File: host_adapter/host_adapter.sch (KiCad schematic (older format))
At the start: 7 parts, among them J1 Conn_01x40_Male, J2 Conn_01x40_Male, J3 Conn_01x02_Male, J4 Connector_PCIe_x16, J5 Conn_01x40_Male, J6 Conn_01x40_Male, J7 Conn_01x02_Male

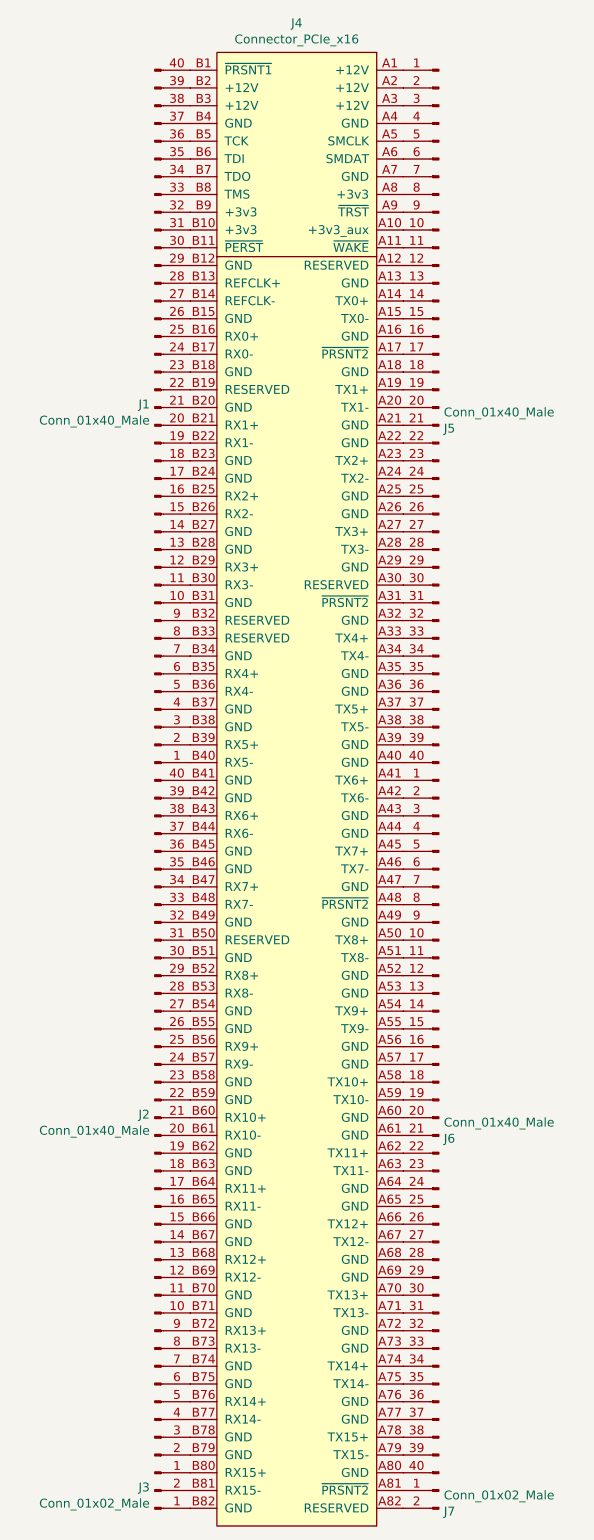
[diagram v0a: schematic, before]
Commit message: Deepen PCIe x16 slot cutout
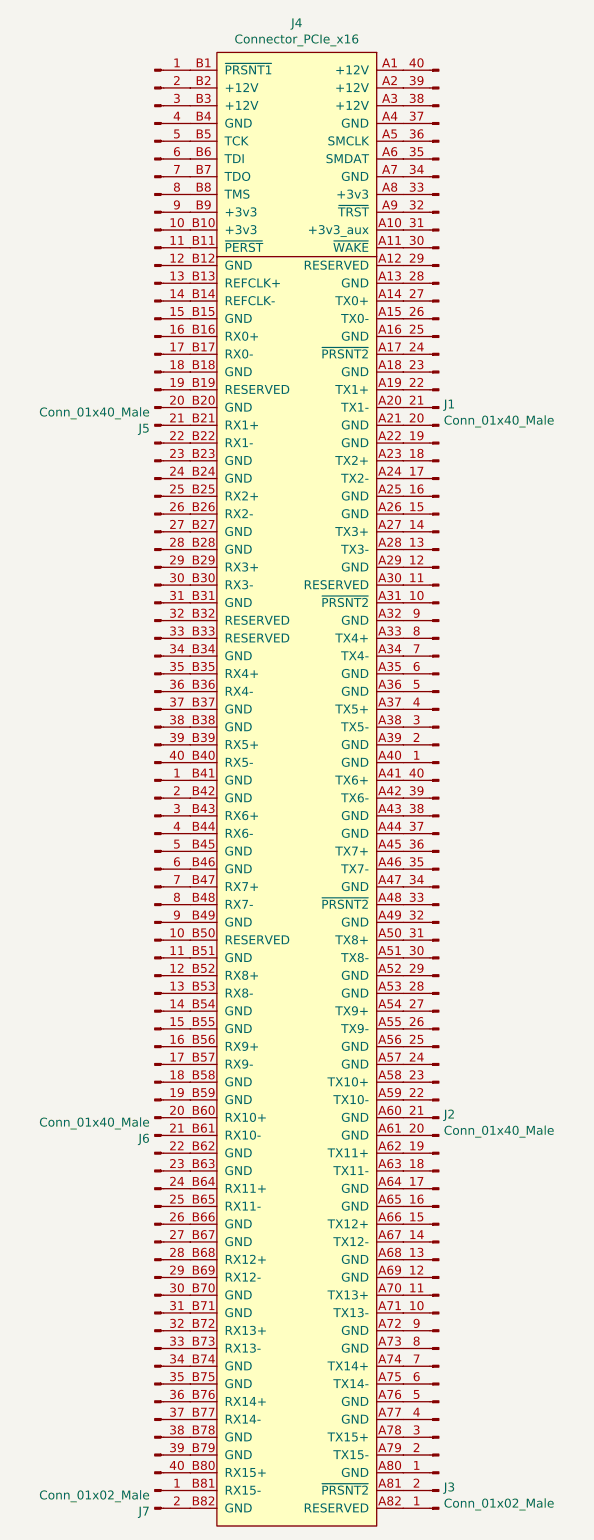
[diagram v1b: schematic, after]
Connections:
- net at J4.A1 (+12V): now also J1.40 (Pin_40); no longer J5.1 (Pin_1)
- net at J4.A10 (+3v3_aux): now also J1.31 (Pin_31); no longer J5.10 (Pin_10)
- net at J4.A11 (~WAKE): now also J1.30 (Pin_30); no longer J5.11 (Pin_11)
- net at J4.A12 (RESERVED): now also J1.29 (Pin_29); no longer J5.12 (Pin_12)
- net at J4.A13 (GND): now also J1.28 (Pin_28); no longer J5.13 (Pin_13)
- net at J4.A14 (TX0+): now also J1.27 (Pin_27); no longer J5.14 (Pin_14)
- net at J4.A15 (TX0-): now also J1.26 (Pin_26); no longer J5.15 (Pin_15)
- net at J4.A16 (GND): now also J1.25 (Pin_25); no longer J5.16 (Pin_16)
- net at J4.A17 (~PRSNT2): now also J1.24 (Pin_24); no longer J5.17 (Pin_17)
- net at J4.A18 (GND): now also J1.23 (Pin_23); no longer J5.18 (Pin_18)
- net at J4.A19 (TX1+): now also J1.22 (Pin_22); no longer J5.19 (Pin_19)
- net at J4.A2 (+12V): now also J1.39 (Pin_39); no longer J5.2 (Pin_2)
- net at J4.A20 (TX1-): now also J1.21 (Pin_21); no longer J5.20 (Pin_20)
- net at J4.A21 (GND): now also J1.20 (Pin_20); no longer J5.21 (Pin_21)
- net at J4.A22 (GND): now also J1.19 (Pin_19); no longer J5.22 (Pin_22)
- net at J4.A23 (TX2+): now also J1.18 (Pin_18); no longer J5.23 (Pin_23)
- net at J4.A24 (TX2-): now also J1.17 (Pin_17); no longer J5.24 (Pin_24)
- net at J4.A25 (GND): now also J1.16 (Pin_16); no longer J5.25 (Pin_25)
- net at J4.A26 (GND): now also J1.15 (Pin_15); no longer J5.26 (Pin_26)
- net at J4.A27 (TX3+): now also J1.14 (Pin_14); no longer J5.27 (Pin_27)
- net at J4.A28 (TX3-): now also J1.13 (Pin_13); no longer J5.28 (Pin_28)
- net at J4.A29 (GND): now also J1.12 (Pin_12); no longer J5.29 (Pin_29)
- net at J4.A3 (+12V): now also J1.38 (Pin_38); no longer J5.3 (Pin_3)
- net at J4.A30 (RESERVED): now also J1.11 (Pin_11); no longer J5.30 (Pin_30)
- net at J4.A31 (~PRSNT2): now also J1.10 (Pin_10); no longer J5.31 (Pin_31)
- net at J4.A32 (GND): now also J1.9 (Pin_9); no longer J5.32 (Pin_32)
- net at J4.A33 (TX4+): now also J1.8 (Pin_8); no longer J5.33 (Pin_33)
- net at J4.A34 (TX4-): now also J1.7 (Pin_7); no longer J5.34 (Pin_34)
- net at J4.A35 (GND): now also J1.6 (Pin_6); no longer J5.35 (Pin_35)
- net at J4.A36 (GND): now also J1.5 (Pin_5); no longer J5.36 (Pin_36)
- net at J4.A37 (TX5+): now also J1.4 (Pin_4); no longer J5.37 (Pin_37)
- net at J4.A38 (TX5-): now also J1.3 (Pin_3); no longer J5.38 (Pin_38)
- net at J4.A39 (GND): now also J1.2 (Pin_2); no longer J5.39 (Pin_39)
- net at J4.A4 (GND): now also J1.37 (Pin_37); no longer J5.4 (Pin_4)
- net at J4.A40 (GND): now also J1.1 (Pin_1); no longer J5.40 (Pin_40)
- net at J4.A41 (TX6+): now also J2.40 (Pin_40); no longer J6.1 (Pin_1)
- net at J4.A42 (TX6-): now also J2.39 (Pin_39); no longer J6.2 (Pin_2)
- net at J4.A43 (GND): now also J2.38 (Pin_38); no longer J6.3 (Pin_3)
- net at J4.A44 (GND): now also J2.37 (Pin_37); no longer J6.4 (Pin_4)
- net at J4.A45 (TX7+): now also J2.36 (Pin_36); no longer J6.5 (Pin_5)
- net at J4.A46 (TX7-): now also J2.35 (Pin_35); no longer J6.6 (Pin_6)
- net at J4.A47 (GND): now also J2.34 (Pin_34); no longer J6.7 (Pin_7)
- net at J4.A48 (~PRSNT2): now also J2.33 (Pin_33); no longer J6.8 (Pin_8)
- net at J4.A49 (GND): now also J2.32 (Pin_32); no longer J6.9 (Pin_9)
- net at J4.A5 (SMCLK): now also J1.36 (Pin_36); no longer J5.5 (Pin_5)
- net at J4.A50 (TX8+): now also J2.31 (Pin_31); no longer J6.10 (Pin_10)
- net at J4.A51 (TX8-): now also J2.30 (Pin_30); no longer J6.11 (Pin_11)
- net at J4.A52 (GND): now also J2.29 (Pin_29); no longer J6.12 (Pin_12)
- net at J4.A53 (GND): now also J2.28 (Pin_28); no longer J6.13 (Pin_13)
- net at J4.A54 (TX9+): now also J2.27 (Pin_27); no longer J6.14 (Pin_14)
- net at J4.A55 (TX9-): now also J2.26 (Pin_26); no longer J6.15 (Pin_15)
- net at J4.A56 (GND): now also J2.25 (Pin_25); no longer J6.16 (Pin_16)
- net at J4.A57 (GND): now also J2.24 (Pin_24); no longer J6.17 (Pin_17)
- net at J4.A58 (TX10+): now also J2.23 (Pin_23); no longer J6.18 (Pin_18)
- net at J4.A59 (TX10-): now also J2.22 (Pin_22); no longer J6.19 (Pin_19)
- net at J4.A6 (SMDAT): now also J1.35 (Pin_35); no longer J5.6 (Pin_6)
- net at J4.A60 (GND): now also J2.21 (Pin_21); no longer J6.20 (Pin_20)
- net at J4.A61 (GND): now also J2.20 (Pin_20); no longer J6.21 (Pin_21)
- net at J4.A62 (TX11+): now also J2.19 (Pin_19); no longer J6.22 (Pin_22)
- net at J4.A63 (TX11-): now also J2.18 (Pin_18); no longer J6.23 (Pin_23)
- net at J4.A64 (GND): now also J2.17 (Pin_17); no longer J6.24 (Pin_24)
- net at J4.A65 (GND): now also J2.16 (Pin_16); no longer J6.25 (Pin_25)
- net at J4.A66 (TX12+): now also J2.15 (Pin_15); no longer J6.26 (Pin_26)
- net at J4.A67 (TX12-): now also J2.14 (Pin_14); no longer J6.27 (Pin_27)
- net at J4.A68 (GND): now also J2.13 (Pin_13); no longer J6.28 (Pin_28)
- net at J4.A69 (GND): now also J2.12 (Pin_12); no longer J6.29 (Pin_29)
- net at J4.A7 (GND): now also J1.34 (Pin_34); no longer J5.7 (Pin_7)
- net at J4.A70 (TX13+): now also J2.11 (Pin_11); no longer J6.30 (Pin_30)
- net at J4.A71 (TX13-): now also J2.10 (Pin_10); no longer J6.31 (Pin_31)
- net at J4.A72 (GND): now also J2.9 (Pin_9); no longer J6.32 (Pin_32)
- net at J4.A73 (GND): now also J2.8 (Pin_8); no longer J6.33 (Pin_33)
- net at J4.A74 (TX14+): now also J2.7 (Pin_7); no longer J6.34 (Pin_34)
- net at J4.A75 (TX14-): now also J2.6 (Pin_6); no longer J6.35 (Pin_35)
- net at J4.A76 (GND): now also J2.5 (Pin_5); no longer J6.36 (Pin_36)
- net at J4.A77 (GND): now also J2.4 (Pin_4); no longer J6.37 (Pin_37)
- net at J4.A78 (TX15+): now also J2.3 (Pin_3); no longer J6.38 (Pin_38)
- net at J4.A79 (TX15-): now also J2.2 (Pin_2); no longer J6.39 (Pin_39)
- net at J4.A8 (+3v3): now also J1.33 (Pin_33); no longer J5.8 (Pin_8)
- net at J4.A80 (GND): now also J2.1 (Pin_1); no longer J6.40 (Pin_40)
- net at J4.A81 (~PRSNT2): now also J3.2 (Pin_2); no longer J7.1 (Pin_1)
- net at J4.A82 (RESERVED): now also J3.1 (Pin_1); no longer J7.2 (Pin_2)
- net at J4.A9 (~TRST): now also J1.32 (Pin_32); no longer J5.9 (Pin_9)
- net at J4.B1 (~PRSNT1): now also J5.1 (Pin_1); no longer J1.40 (Pin_40)
- net at J4.B10 (+3v3): now also J5.10 (Pin_10); no longer J1.31 (Pin_31)
- net at J4.B11 (~PERST): now also J5.11 (Pin_11); no longer J1.30 (Pin_30)
- net at J4.B12 (GND): now also J5.12 (Pin_12); no longer J1.29 (Pin_29)
- net at J4.B13 (REFCLK+): now also J5.13 (Pin_13); no longer J1.28 (Pin_28)
- net at J4.B14 (REFCLK-): now also J5.14 (Pin_14); no longer J1.27 (Pin_27)
- net at J4.B15 (GND): now also J5.15 (Pin_15); no longer J1.26 (Pin_26)
- net at J4.B16 (RX0+): now also J5.16 (Pin_16); no longer J1.25 (Pin_25)
- net at J4.B17 (RX0-): now also J5.17 (Pin_17); no longer J1.24 (Pin_24)
- net at J4.B18 (GND): now also J5.18 (Pin_18); no longer J1.23 (Pin_23)
- net at J4.B19 (RESERVED): now also J5.19 (Pin_19); no longer J1.22 (Pin_22)
- net at J4.B2 (+12V): now also J5.2 (Pin_2); no longer J1.39 (Pin_39)
- net at J4.B20 (GND): now also J5.20 (Pin_20); no longer J1.21 (Pin_21)
- net at J4.B21 (RX1+): now also J5.21 (Pin_21); no longer J1.20 (Pin_20)
- net at J4.B22 (RX1-): now also J5.22 (Pin_22); no longer J1.19 (Pin_19)
- net at J4.B23 (GND): now also J5.23 (Pin_23); no longer J1.18 (Pin_18)
- net at J4.B24 (GND): now also J5.24 (Pin_24); no longer J1.17 (Pin_17)
- net at J4.B25 (RX2+): now also J5.25 (Pin_25); no longer J1.16 (Pin_16)
- net at J4.B26 (RX2-): now also J5.26 (Pin_26); no longer J1.15 (Pin_15)
- net at J4.B27 (GND): now also J5.27 (Pin_27); no longer J1.14 (Pin_14)
- net at J4.B28 (GND): now also J5.28 (Pin_28); no longer J1.13 (Pin_13)
- net at J4.B29 (RX3+): now also J5.29 (Pin_29); no longer J1.12 (Pin_12)
- net at J4.B3 (+12V): now also J5.3 (Pin_3); no longer J1.38 (Pin_38)
- net at J4.B30 (RX3-): now also J5.30 (Pin_30); no longer J1.11 (Pin_11)
- net at J4.B31 (GND): now also J5.31 (Pin_31); no longer J1.10 (Pin_10)
- net at J4.B32 (RESERVED): now also J5.32 (Pin_32); no longer J1.9 (Pin_9)
- net at J4.B33 (RESERVED): now also J5.33 (Pin_33); no longer J1.8 (Pin_8)
- net at J4.B34 (GND): now also J5.34 (Pin_34); no longer J1.7 (Pin_7)
- net at J4.B35 (RX4+): now also J5.35 (Pin_35); no longer J1.6 (Pin_6)
- net at J4.B36 (RX4-): now also J5.36 (Pin_36); no longer J1.5 (Pin_5)
- net at J4.B37 (GND): now also J5.37 (Pin_37); no longer J1.4 (Pin_4)
- net at J4.B38 (GND): now also J5.38 (Pin_38); no longer J1.3 (Pin_3)
- net at J4.B39 (RX5+): now also J5.39 (Pin_39); no longer J1.2 (Pin_2)
- net at J4.B4 (GND): now also J5.4 (Pin_4); no longer J1.37 (Pin_37)
- net at J4.B40 (RX5-): now also J5.40 (Pin_40); no longer J1.1 (Pin_1)
- net at J4.B41 (GND): now also J6.1 (Pin_1); no longer J2.40 (Pin_40)
- net at J4.B42 (GND): now also J6.2 (Pin_2); no longer J2.39 (Pin_39)
- net at J4.B43 (RX6+): now also J6.3 (Pin_3); no longer J2.38 (Pin_38)
- net at J4.B44 (RX6-): now also J6.4 (Pin_4); no longer J2.37 (Pin_37)
- net at J4.B45 (GND): now also J6.5 (Pin_5); no longer J2.36 (Pin_36)
- net at J4.B46 (GND): now also J6.6 (Pin_6); no longer J2.35 (Pin_35)
- net at J4.B47 (RX7+): now also J6.7 (Pin_7); no longer J2.34 (Pin_34)
- net at J4.B48 (RX7-): now also J6.8 (Pin_8); no longer J2.33 (Pin_33)
- net at J4.B49 (GND): now also J6.9 (Pin_9); no longer J2.32 (Pin_32)
- net at J4.B5 (TCK): now also J5.5 (Pin_5); no longer J1.36 (Pin_36)
- net at J4.B50 (RESERVED): now also J6.10 (Pin_10); no longer J2.31 (Pin_31)
- net at J4.B51 (GND): now also J6.11 (Pin_11); no longer J2.30 (Pin_30)
- net at J4.B52 (RX8+): now also J6.12 (Pin_12); no longer J2.29 (Pin_29)
- net at J4.B53 (RX8-): now also J6.13 (Pin_13); no longer J2.28 (Pin_28)
- net at J4.B54 (GND): now also J6.14 (Pin_14); no longer J2.27 (Pin_27)
- net at J4.B55 (GND): now also J6.15 (Pin_15); no longer J2.26 (Pin_26)
- net at J4.B56 (RX9+): now also J6.16 (Pin_16); no longer J2.25 (Pin_25)
- net at J4.B57 (RX9-): now also J6.17 (Pin_17); no longer J2.24 (Pin_24)
- net at J4.B58 (GND): now also J6.18 (Pin_18); no longer J2.23 (Pin_23)
- net at J4.B59 (GND): now also J6.19 (Pin_19); no longer J2.22 (Pin_22)
- net at J4.B6 (TDI): now also J5.6 (Pin_6); no longer J1.35 (Pin_35)
- net at J4.B60 (RX10+): now also J6.20 (Pin_20); no longer J2.21 (Pin_21)
- net at J4.B61 (RX10-): now also J6.21 (Pin_21); no longer J2.20 (Pin_20)
- net at J4.B62 (GND): now also J6.22 (Pin_22); no longer J2.19 (Pin_19)
- net at J4.B63 (GND): now also J6.23 (Pin_23); no longer J2.18 (Pin_18)
- net at J4.B64 (RX11+): now also J6.24 (Pin_24); no longer J2.17 (Pin_17)
- net at J4.B65 (RX11-): now also J6.25 (Pin_25); no longer J2.16 (Pin_16)
- net at J4.B66 (GND): now also J6.26 (Pin_26); no longer J2.15 (Pin_15)
- net at J4.B67 (GND): now also J6.27 (Pin_27); no longer J2.14 (Pin_14)
- net at J4.B68 (RX12+): now also J6.28 (Pin_28); no longer J2.13 (Pin_13)
- net at J4.B69 (RX12-): now also J6.29 (Pin_29); no longer J2.12 (Pin_12)
- net at J4.B7 (TDO): now also J5.7 (Pin_7); no longer J1.34 (Pin_34)
- net at J4.B70 (GND): now also J6.30 (Pin_30); no longer J2.11 (Pin_11)
- net at J4.B71 (GND): now also J6.31 (Pin_31); no longer J2.10 (Pin_10)
- net at J4.B72 (RX13+): now also J6.32 (Pin_32); no longer J2.9 (Pin_9)
- net at J4.B73 (RX13-): now also J6.33 (Pin_33); no longer J2.8 (Pin_8)
- net at J4.B74 (GND): now also J6.34 (Pin_34); no longer J2.7 (Pin_7)
- net at J4.B75 (GND): now also J6.35 (Pin_35); no longer J2.6 (Pin_6)
- net at J4.B76 (RX14+): now also J6.36 (Pin_36); no longer J2.5 (Pin_5)
- net at J4.B77 (RX14-): now also J6.37 (Pin_37); no longer J2.4 (Pin_4)
- net at J4.B78 (GND): now also J6.38 (Pin_38); no longer J2.3 (Pin_3)
- net at J4.B79 (GND): now also J6.39 (Pin_39); no longer J2.2 (Pin_2)
- net at J4.B8 (TMS): now also J5.8 (Pin_8); no longer J1.33 (Pin_33)
- net at J4.B80 (RX15+): now also J6.40 (Pin_40); no longer J2.1 (Pin_1)
- net at J4.B81 (RX15-): now also J7.1 (Pin_1); no longer J3.2 (Pin_2)
- net at J4.B82 (GND): now also J7.2 (Pin_2); no longer J3.1 (Pin_1)
- net at J4.B9 (+3v3): now also J5.9 (Pin_9); no longer J1.32 (Pin_32)
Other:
- moved on the sheet: J1, J2, J3, J5, J6, J7
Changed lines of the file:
@@
 L Connector:Conn_01x40_Male J1
 U 1 1 5F4FABD2
-P 3350 3350
-F 0 "J1" H 3322 3232 50  0000 R CNN
-F 1 "Conn_01x40_Male" H 3322 3323 50  0000 R CNN
-F 2 "Connector_PinHeader_EdgeLaunch_2.54mm:Connector_PinHeader_EdgeLaunch_2,54mm_01x40" H 3350 3350 50  0001 C CNN
-F 3 "~" H 3350 3350 50  0001 C CNN
-	1    3350 3350
-	1    0    0    1
+P 4950 3350
+F 0 "J1" H 4922 3232 50  0000 R CNN
+F 1 "Conn_01x40_Male" H 4922 3323 50  0000 R CNN
+F 2 "Connector_PinHeader_EdgeLaunch_2.54mm:Connector_PinHeader_EdgeLaunch_2,54mm_01x40" H 4950 3350 50  0001 C CNN
+F 3 "~" H 4950 3350 50  0001 C CNN
+	1    4950 3350
+	-1   0    0    1
 $EndComp
 $Comp
 L Connector:Conn_01x40_Male J2
 U 1 1 5F500F7E
-P 3350 7350
-F 0 "J2" H 3322 7232 50  0000 R CNN
-F 1 "Conn_01x40_Male" H 3322 7323 50  0000 R CNN
-F 2 "Connector_PinHeader_EdgeLaunch_2.54mm:Connector_PinHeader_EdgeLaunch_2,54mm_01x40" H 3350 7350 50  0001 C CNN
-F 3 "~" H 3350 7350 50  0001 C CNN
-	1    3350 7350
-	1    0    0    1
+P 4950 7350
+F 0 "J2" H 4922 7232 50  0000 R CNN
+F 1 "Conn_01x40_Male" H 4922 7323 50  0000 R CNN
+F 2 "Connector_PinHeader_EdgeLaunch_2.54mm:Connector_PinHeader_EdgeLaunch_2,54mm_01x40" H 4950 7350 50  0001 C CNN
+F 3 "~" H 4950 7350 50  0001 C CNN
+	1    4950 7350
+	-1   0    0    1
 $EndComp
 $Comp
 L Connector:Conn_01x40_Male J5
 U 1 1 5F50749D
-P 4950 3250
-F 0 "J5" H 4922 3132 50  0000 R CNN
-F 1 "Conn_01x40_Male" H 4922 3223 50  0000 R CNN
-F 2 "Connector_PinHeader_EdgeLaunch_2.54mm:Connector_PinHeader_EdgeLaunch_2,54mm_01x40" H 4950 3250 50  0001 C CNN
-F 3 "~" H 4950 3250 50  0001 C CNN
-	1    4950 3250
-	-1   0    0    -1
+P 3350 3250
+F 0 "J5" H 3322 3132 50  0000 R CNN
+F 1 "Conn_01x40_Male" H 3322 3223 50  0000 R CNN
+F 2 "Connector_PinHeader_EdgeLaunch_2.54mm:Connector_PinHeader_EdgeLaunch_2,54mm_01x40" H 3350 3250 50  0001 C CNN
+F 3 "~" H 3350 3250 50  0001 C CNN
+	1    3350 3250
+	1    0    0    -1
 $EndComp
 $Comp
 L Connector:Conn_01x40_Male J6
 U 1 1 5F508CF8
-P 4950 7250
-F 0 "J6" H 4922 7132 50  0000 R CNN
-F 1 "Conn_01x40_Male" H 4922 7223 50  0000 R CNN
-F 2 "Connector_PinHeader_EdgeLaunch_2.54mm:Connector_PinHeader_EdgeLaunch_2,54mm_01x40" H 4950 7250 50  0001 C CNN
-F 3 "~" H 4950 7250 50  0001 C CNN
-	1    4950 7250
-	-1   0    0    -1
+P 3350 7250
+F 0 "J6" H 3322 7132 50  0000 R CNN
+F 1 "Conn_01x40_Male" H 3322 7223 50  0000 R CNN
+F 2 "Connector_PinHeader_EdgeLaunch_2.54mm:Connector_PinHeader_EdgeLaunch_2,54mm_01x40" H 3350 7250 50  0001 C CNN
+F 3 "~" H 3350 7250 50  0001 C CNN
+	1    3350 7250
+	1    0    0    -1
 $EndComp
 $Comp
 L Connector:Conn_01x02_Male J3
 U 1 1 5F50A12B
-P 3350 9450
-F 0 "J3" H 3322 9332 50  0000 R CNN
-F 1 "Conn_01x02_Male" H 3322 9423 50  0000 R CNN
-F 2 "Connector_PinHeader_EdgeLaunch_2.54mm:Connector_PinHeader_EdgeLaunch_2,54mm_01x02" H 3350 9450 50  0001 C CNN
-F 3 "~" H 3350 9450 50  0001 C CNN
-	1    3350 9450
-	1    0    0    1
+P 4950 9450
+F 0 "J3" H 4922 9332 50  0000 R CNN
+F 1 "Conn_01x02_Male" H 4922 9423 50  0000 R CNN
+F 2 "Connector_PinHeader_EdgeLaunch_2.54mm:Connector_PinHeader_EdgeLaunch_2,54mm_01x02" H 4950 9450 50  0001 C CNN
+F 3 "~" H 4950 9450 50  0001 C CNN
+	1    4950 9450
+	-1   0    0    1
 $EndComp
 $Comp
 L Connector:Conn_01x02_Male J7
 U 1 1 5F50ADB0
-P 4950 9350
-F 0 "J7" H 4922 9232 50  0000 R CNN
-F 1 "Conn_01x02_Male" H 4922 9323 50  0000 R CNN
-F 2 "Connector_PinHeader_EdgeLaunch_2.54mm:Connector_PinHeader_EdgeLaunch_2,54mm_01x02" H 4950 9350 50  0001 C CNN
-F 3 "~" H 4950 9350 50  0001 C CNN
-	1    4950 9350
-	-1   0    0    -1
+P 3350 9350
+F 0 "J7" H 3322 9232 50  0000 R CNN
+F 1 "Conn_01x02_Male" H 3322 9323 50  0000 R CNN
+F 2 "Connector_PinHeader_EdgeLaunch_2.54mm:Connector_PinHeader_EdgeLaunch_2,54mm_01x02" H 3350 9350 50  0001 C CNN
+F 3 "~" H 3350 9350 50  0001 C CNN
+	1    3350 9350
+	1    0    0    -1
 $EndComp
 $EndSCHEMATC
